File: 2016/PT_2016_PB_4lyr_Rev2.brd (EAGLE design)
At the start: 154.7 x 201.9 mm, 148 parts, among them M1+ ANDERSON_POWERPOLEPP45_PCB_HO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, M1- ANDERSON_POWERPOLEPP45_PCB_HO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, M2+ ANDERSON_POWERPOLEPP45_PCB_HO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, M2- ANDERSON_POWERPOLEPP45_PCB_HO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, M2-1 ANDERSON_POWERPOLEPP45_PCB_HO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, M2-2 ANDERSON_POWERPOLEPP45_PCB_HO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, M2-3 ANDERSON_POWERPOLEPP45_PCB_HO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, M2-4 ANDERSON_POWERPOLEPP45_PCB_HO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, M3+ ANDERSON_POWERPOLEPP45_PCB_HO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, M3- ANDERSON_POWERPOLEPP45_PCB_HO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, M4+ ANDERSON_POWERPOLEPP45_PCB_HO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, M4- ANDERSON_POWERPOLEPP45_PCB_HO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, M5+ ANDERSON_POWERPOLEPP45_PCB_HO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, M5- ANDERSON_POWERPOLEPP45_PCB_HO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, M6+ ANDERSON_POWERPOLEPP45_PCB_HO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, M6- ANDERSON_POWERPOLEPP45_PCB_HO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, Q1 Q_IRFS7437PbF, Q11 Q_IRFS7437PbF, Q12 2N7002, Q14 Q_IRFS7437PbF, Q16 Q_IRFS7437PbF, Q2 2N7002, Q20 Q_IRFS7437PbF, Q6 Q_IRFS7437PbF, Q7 Q_IRFS7437PbF, Q9 Q_IRFS7437PbF, X1 22-23-2041

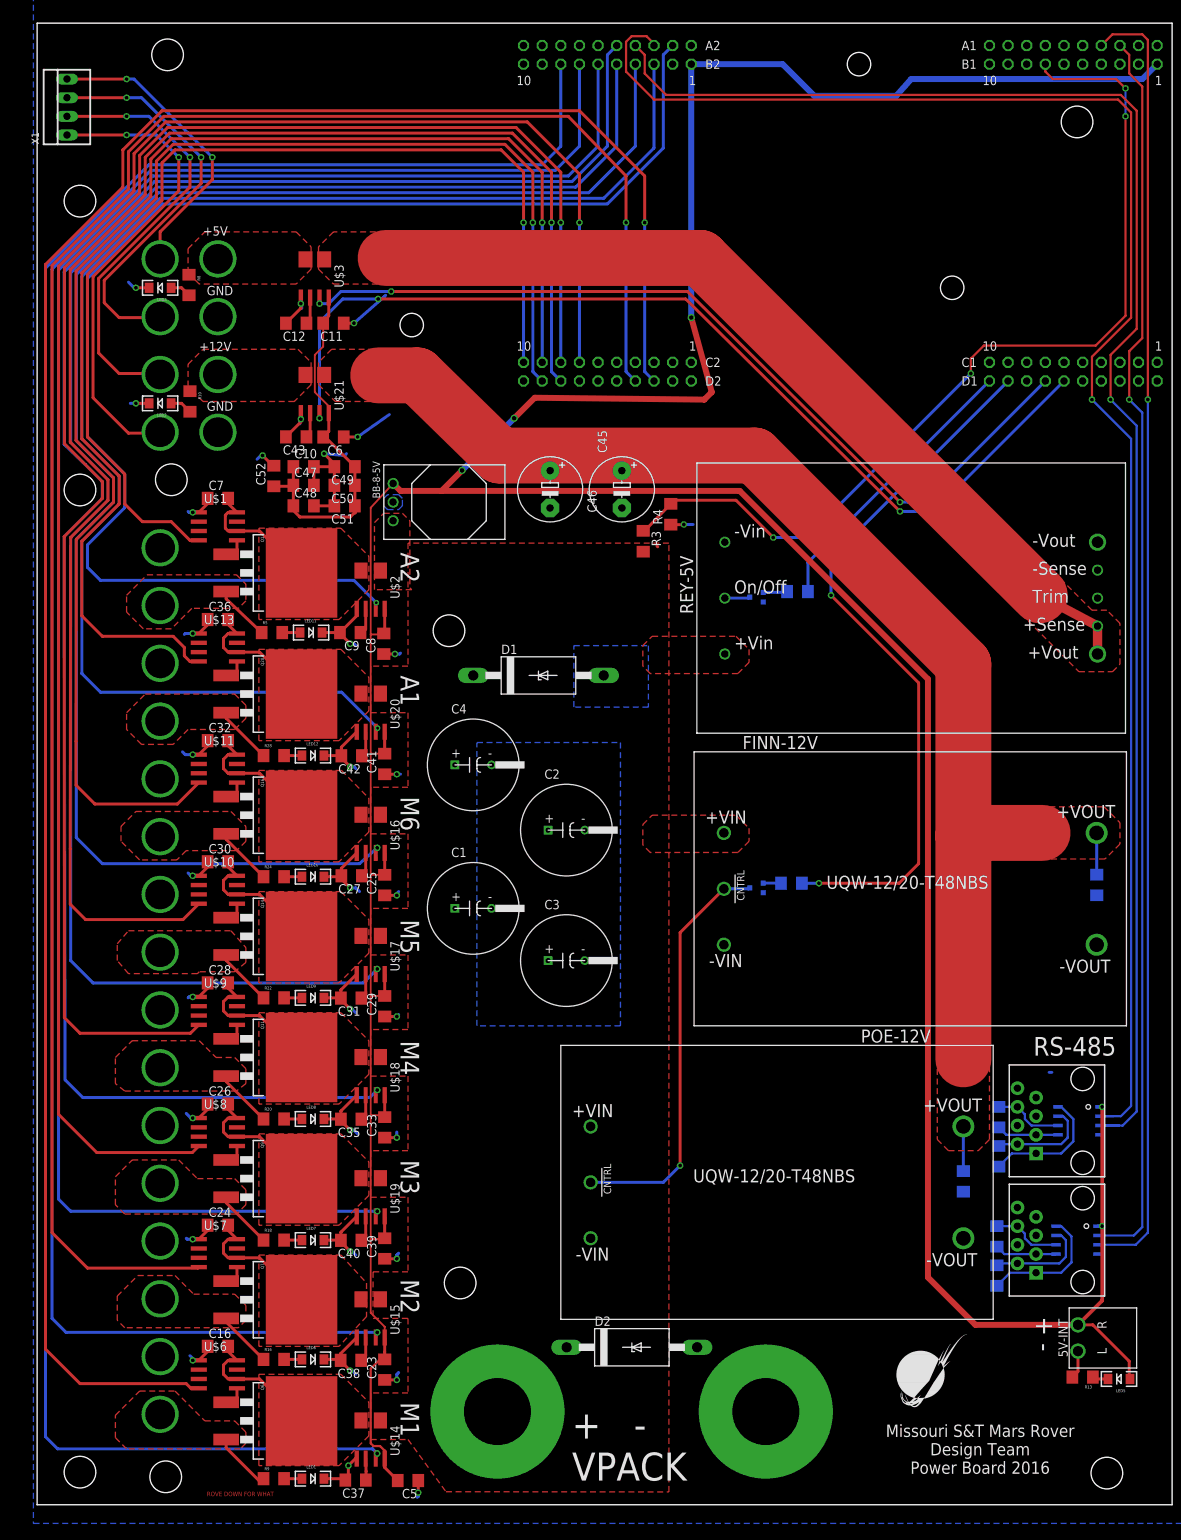
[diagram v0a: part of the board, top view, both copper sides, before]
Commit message: Jake started routing 4 layer board
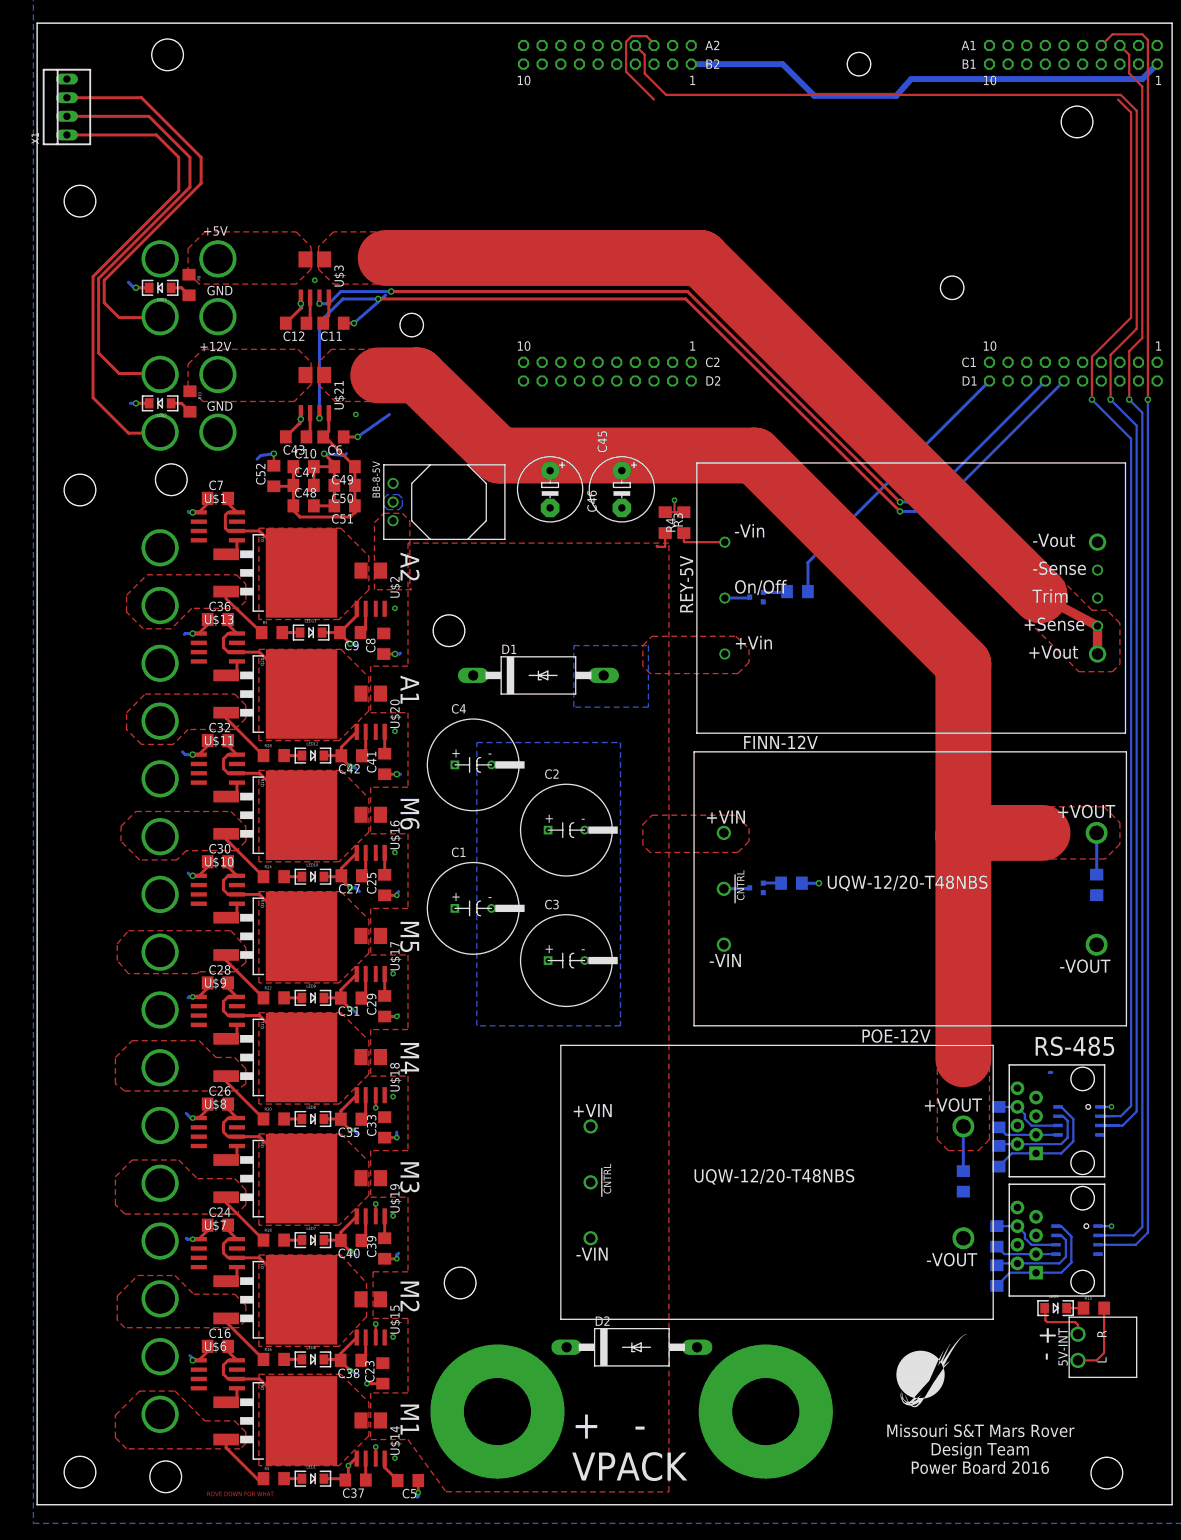
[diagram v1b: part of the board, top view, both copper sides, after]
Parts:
- moved LED5 13.0 mm to (134.0, 23.0), turned to 0 degrees
- moved R13 9.52 mm to (139.2, 23.0), turned to 0 degrees
- moved R3 3.93 mm to (80.8, 130.0)
- moved R4 2.11 mm to (83.3, 130.0)
- moved 5V-INT 1.27 mm to (137.0, 17.7)
- moved C23 0.57 mm to (42.3, 14.1)
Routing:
- net +5V: track 617.1 -> 132.4 mm, vias 5 -> 12
- net M1-SIG: track 296.4 -> 0.00 mm, vias 1 -> 0
- net M2-SIG: track 275.4 -> 0.00 mm, vias 1 -> 0
- net M3-SIG: track 247.9 -> 0.00 mm, vias 1 -> 0
- net M4-SIG: track 233.1 -> 0.00 mm, vias 1 -> 0
- net M6-IMEAS: track 220.6 -> 0.90 mm, vias 1 -> 0
- net M5-SIG: track 217.5 -> 0.00 mm, vias 1 -> 0
- net AUX_P-IMEAS: track 198.9 -> 0.00 mm, vias 1 -> 0
- net M6-SIG: track 195.1 -> 0.00 mm, vias 1 -> 0
- net AUX_P2-IMEAS: track 186.3 -> 0.00 mm, vias 1 -> 0
- net AUX_P-SIG: track 172.4 -> 0.00 mm, vias 1 -> 0
- net AUX_P2-SIG: track 142.1 -> 0.00 mm, vias 1 -> 0
- net RX2: track 226.5 -> 163.2 mm
- net M5-IMEAS: track 235.4 -> 179.4 mm, vias 1 -> 0
- net M4-IMEAS: track 254.7 -> 202.2 mm
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- added copper zone on layer 2, net +5V
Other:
- board text added: "obama did 9/11"

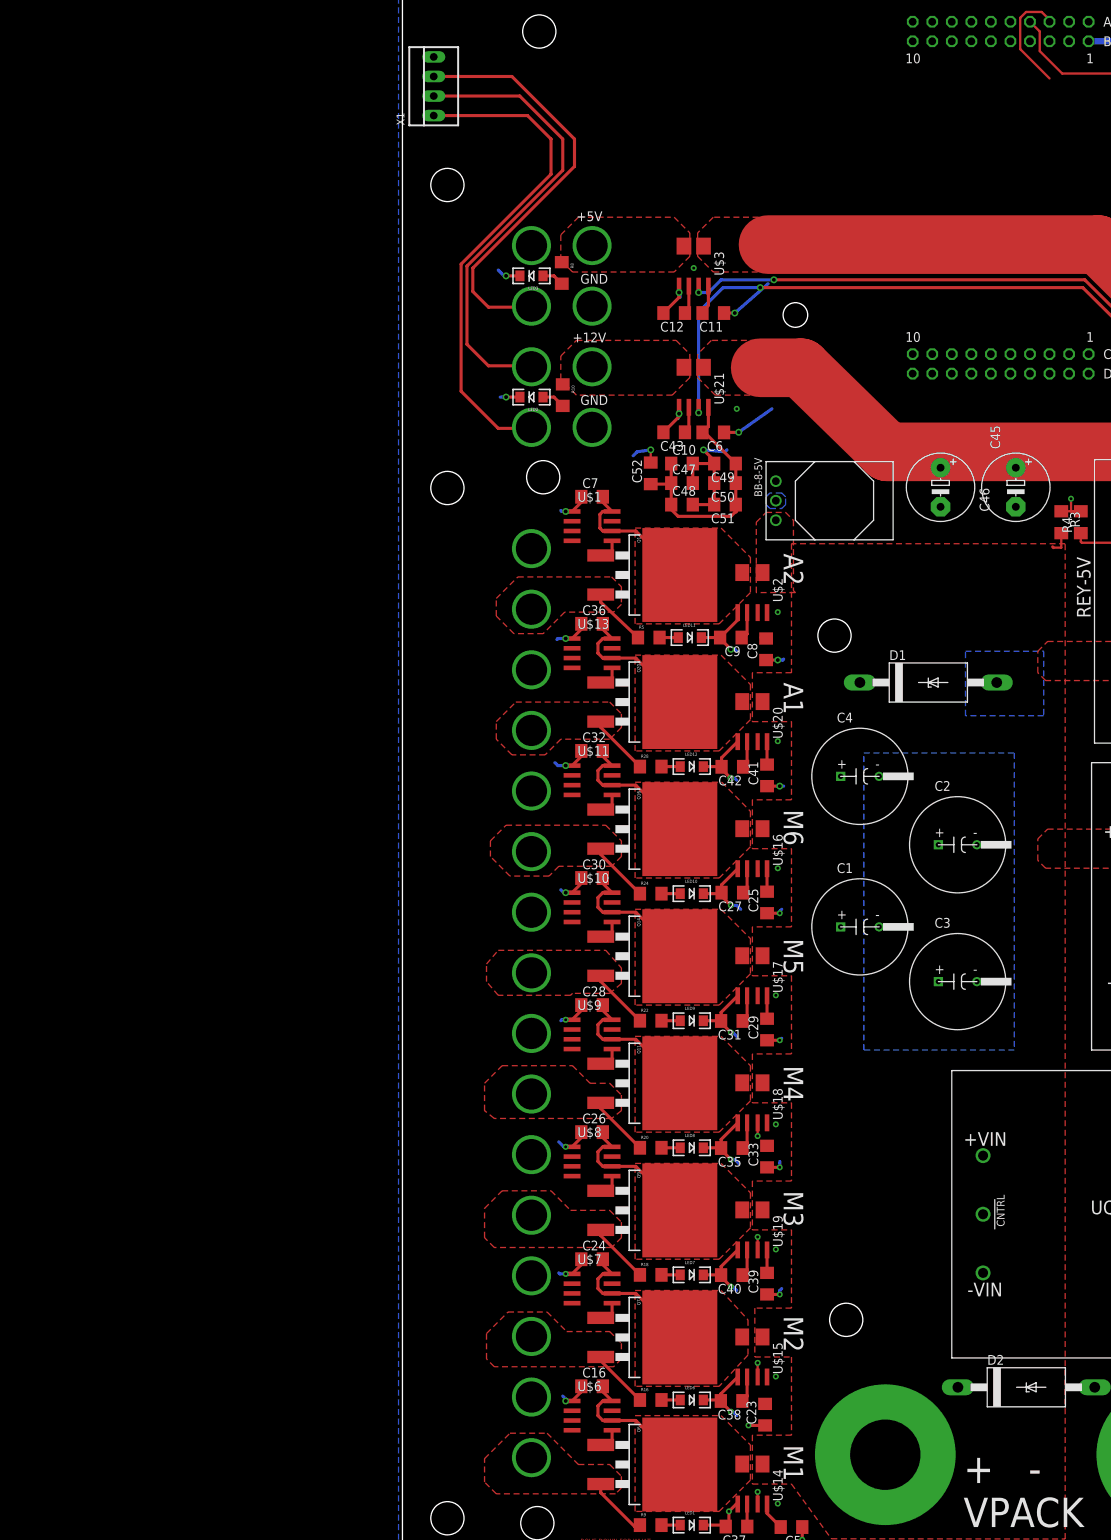
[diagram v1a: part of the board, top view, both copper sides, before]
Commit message: Added space for addition mounting wings and started moving components
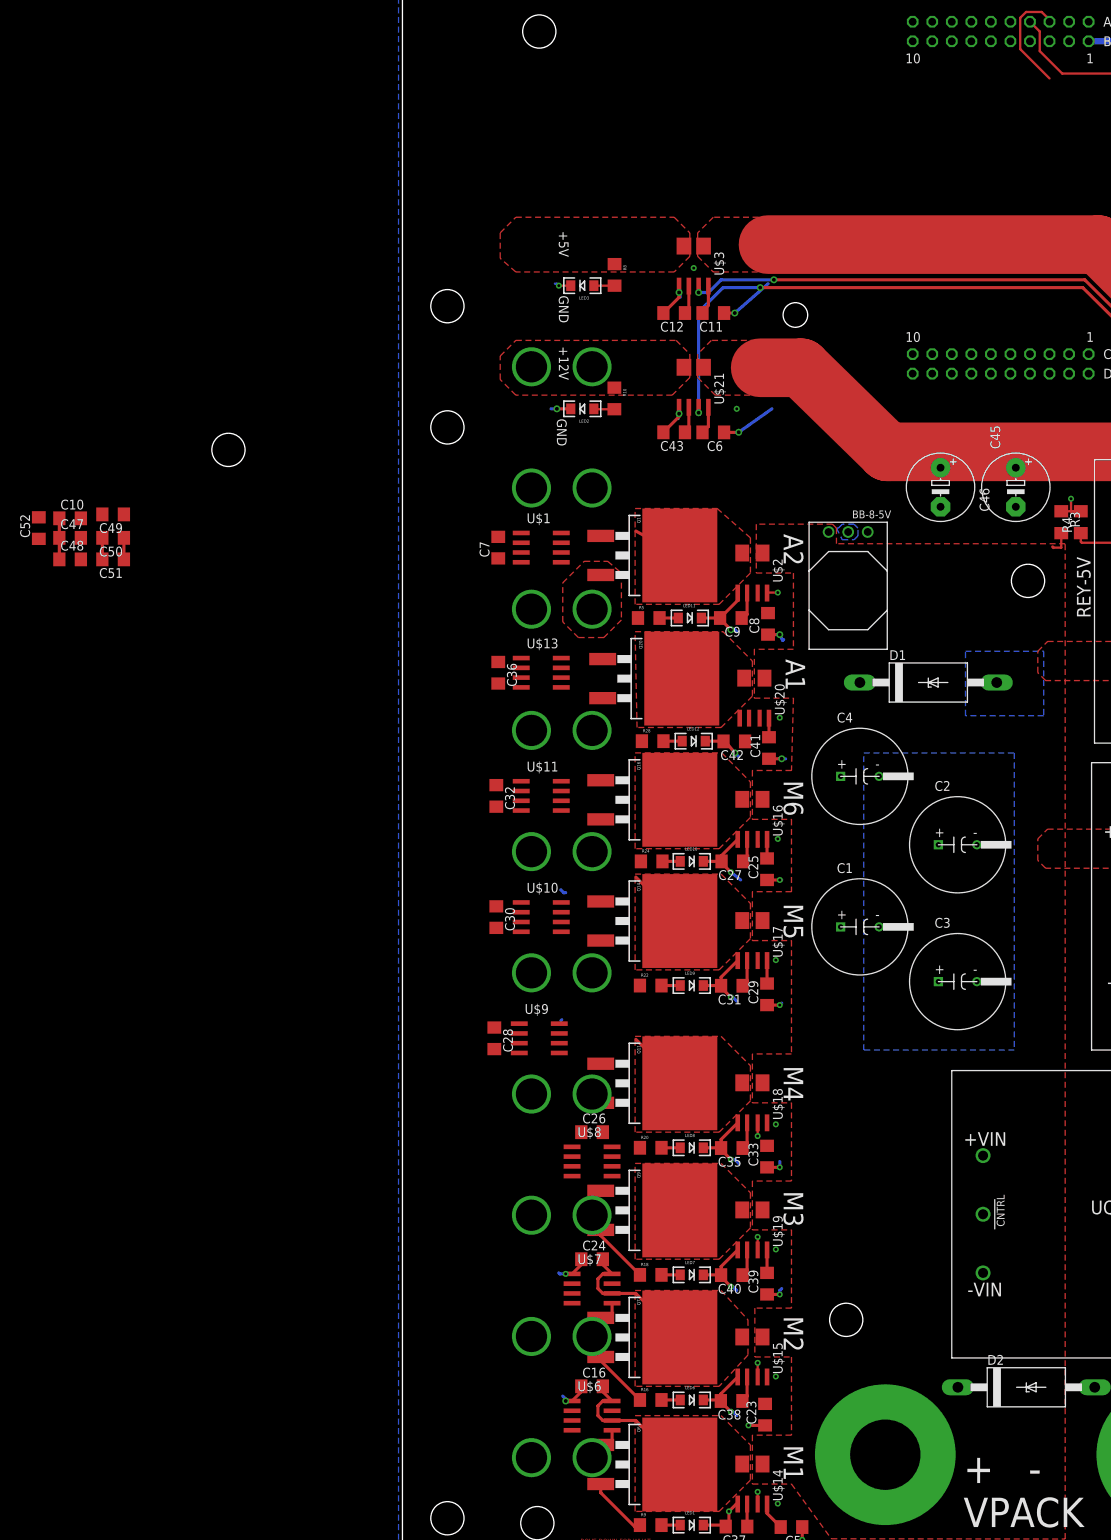
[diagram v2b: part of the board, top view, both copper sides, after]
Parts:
- removed M2-1, M2-2, M2-3, M2-4: ANDERSON_POWERPOLEPP45_PCB_HORIZ_RIGHT, MRDT-Connectors:APP45_PCB_HORIZ_RIGHT
- removed X1: 22-23-2041, con-molex:22-23-2041
- AUX1+, AUX2+, M1+, M2+, M3+, M4+, M5+, M6+: value ANDERSON_POWERPOLEPP45_PCB_HORIZ_RIGHT -> ANDERSON_POWERPOLEPP45_PCB_HORIZ_RIGHT_2HIGH; device MRDT-Connectors:APP45_PCB_HORIZ_RIGHT -> MRDT-Connectors:APP45_PCB_HORIZ_RIGHT_2HIGH
- C16, C24, C26, C28, C30, C32, C36, C7: value 10µF -> .1µF
- U$28, U$29: value ANDERSON_POWERPOLEPP45_PCB_HORIZ_RIGHT_2HIGH -> ANDERSON_POWERPOLEPP45_PCB_HORIZ_RIGHT; device MRDT-Connectors:APP45_PCB_HORIZ_RIGHT_2HIGH -> MRDT-Connectors:APP45_PCB_HORIZ_RIGHT
- moved C51 79.8 mm to (-42.4, 125.2)
- moved C48 79.8 mm to (-48.0, 125.2)
- moved C50 79.8 mm to (-42.4, 128.0)
- moved C10 79.8 mm to (-48.0, 130.6)
- moved C47 79.8 mm to (-48.0, 128.0)
- moved C52 79.8 mm to (-52.1, 129.3)
- moved C49 79.8 mm to (-42.4, 131.1)
- moved U$25 15.7 mm to (8.38, 162.1)
- moved U$26 15.7 mm to (-16.3, 130.6)
- moved U$27 15.7 mm to (-16.3, 146.3)
- moved C7 13.9 mm to (7.62, 126.7), turned to 90 degrees
- moved C32 13.7 mm to (7.37, 94.5), turned to 270 degrees
- moved C36 13.7 mm to (7.62, 110.5), turned to 270 degrees
- moved C30 13.4 mm to (7.37, 78.7), turned to 270 degrees
- moved C28 13.4 mm to (7.11, 63.0), turned to 270 degrees
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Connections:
- removed net N$11: M2-2.P$1, X1.1
- removed net N$3: M2-3.P$1, X1.4
- removed net N$5: M2-1.P$1, X1.3
- removed net N$8: M2-4.P$1, X1.2
- net GND: now also U$28.P$1, U$29.P$1; no longer U$28.P$2, U$29.P$2
- net N$10: now also AUX2+.P$2; no longer AUX2+.P$1
- net N$29: now also M2+.P$2; no longer M2+.P$1
- net N$41: now also M1+.P$2; no longer M1+.P$1
- net N$45: now also M3+.P$2; no longer M3+.P$1
- net N$55: now also M4+.P$2; no longer M4+.P$1
- net N$61: now also M5+.P$2; no longer M5+.P$1
- net N$67: now also M6+.P$2; no longer M6+.P$1
- net N$79: now also AUX1+.P$2; no longer AUX1+.P$1
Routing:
- net N$11: track 65.3 -> 0.00 mm
- net N$8: track 60.5 -> 0.00 mm
- net N$5: track 55.5 -> 0.00 mm
- net GND: track 195.7 -> 145.2 mm, vias 32 -> 24
- net +5V: track 132.4 -> 111.2 mm
- net N$66: track 19.0 -> 0.00 mm
- net N$78: track 19.0 -> 0.00 mm
- net N$44: track 19.0 -> 0.00 mm
- net N$9: track 18.8 -> 6.54 mm
- net N$54: track 19.0 -> 8.08 mm
- net N$60: track 19.0 -> 8.08 mm
- net N$79: track 7.95 -> 0.00 mm
- net N$61: track 7.95 -> 0.00 mm
- net N$67: track 7.95 -> 0.00 mm
- net N$10: track 7.67 -> 0.00 mm
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- removed copper zone on layer 1, net N$29
- removed copper zone on layer 1, net N$41
- removed copper zone on layer 1, net N$45
- removed copper zone on layer 1, net N$55
- removed copper zone on layer 1, net N$61
- removed copper zone on layer 1, net N$67
- removed copper zone on layer 1, net N$79
